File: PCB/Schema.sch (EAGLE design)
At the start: 15 parts, among them J1 PINHD-2X5, J2 PINHD-2X5, Q1 NMOSFET, Q2 NMOSFET, Q3 NMOSFET, Q4 NMOSFET

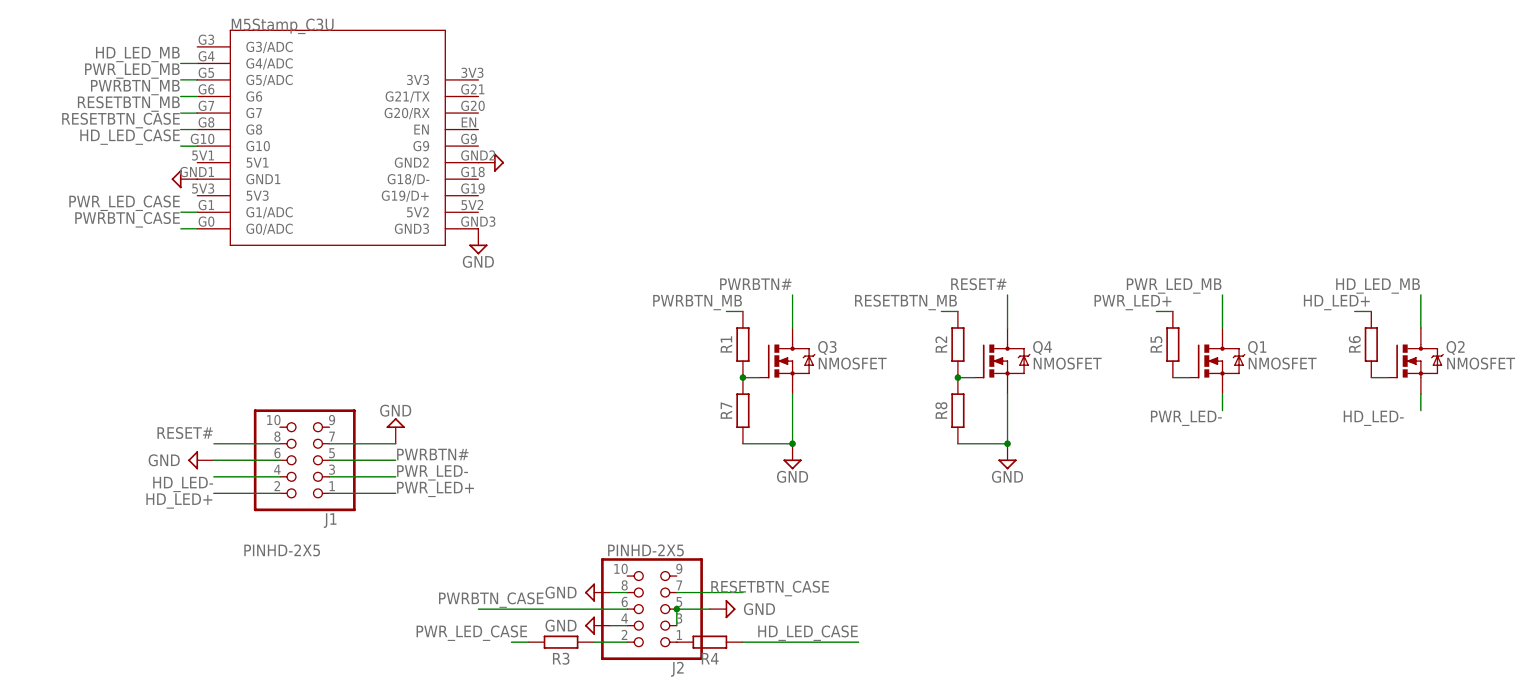
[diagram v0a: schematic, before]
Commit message: 基板を更新: LEDを5Vから駆動するようにしたりRESET / HDDLEDを触らないようにしたり
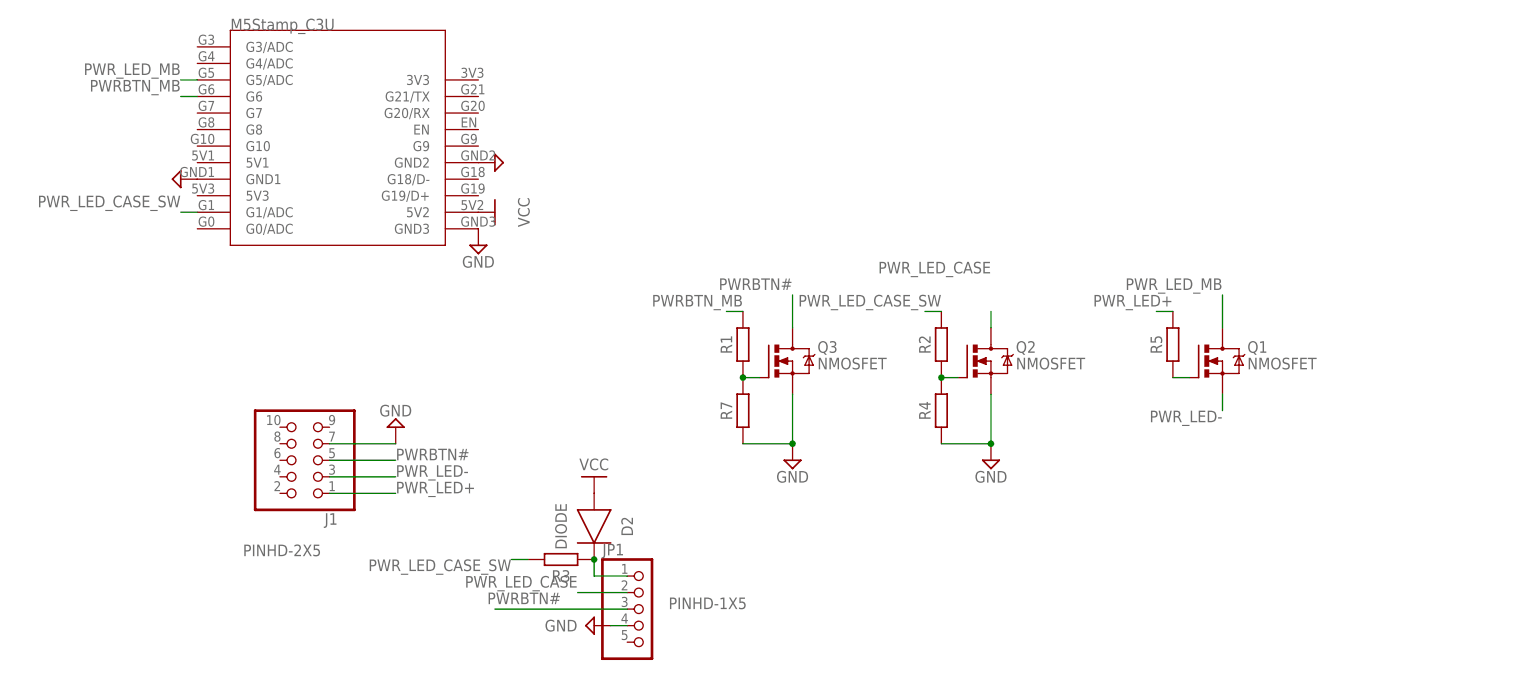
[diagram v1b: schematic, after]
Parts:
- removed J2: PINHD-2X5, Connector:PINHD-2X5
- removed Q4: NMOSFET, Transistor:NMOSFET_SOT23-GSD
- removed R6, R8: (no value), Resistor:R_CHIP-0603(1608-METRIC)
- added D2: DIODE, Diode:DIODE_DO-219-AB(SOD123F)
- added JP1: PINHD-1X5, Connector:PINHD-1X5
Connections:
- removed net HD_LED+: J1.2, R6.2
- removed net HD_LED-: J1.4, Q2.S
- removed net HD_LED_CASE: R4.1, U$1.G10
- removed net HD_LED_MB: Q2.D, U$1.G4/ADC
- removed net N$3: J2.1, R4.2
- removed net N$6: Q2.G, R6.1
- removed net PWRBTN_CASE: J2.6, U$1.G0/ADC
- removed net RESET#: J1.8, Q4.D
- removed net RESETBTN_CASE: J2.7, U$1.G8
- removed net RESETBTN_MB: R2.2, U$1.G7
- new net PWR_LED_CASE_SW: R2.2, R3.2, U$1.G1/ADC
- new net VCC: D2.A, U$1.5V2
- net GND: now also JP1.4, Q2.S, R4.1; no longer J1.6, J2.3, J2.4, J2.5, J2.8, Q4.S, R8.1
- net N$2: now also Q2.G, R4.2; no longer Q4.G, R8.2
- net N$4: now also D2.C, JP1.1, R3.1; no longer J2.2, R3.2
- net PWRBTN#: now also JP1.3
- net PWR_LED_CASE: now also JP1.2, Q2.D; no longer R3.1, U$1.G1/ADC
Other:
- moved on the sheet: Q2, R2, R3, R4
